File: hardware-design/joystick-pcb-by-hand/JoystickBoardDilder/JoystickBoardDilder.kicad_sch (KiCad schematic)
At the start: 2 parts, among them SW1 K1-1506SN-01, SW1Header1 Conn_01x06_Pin

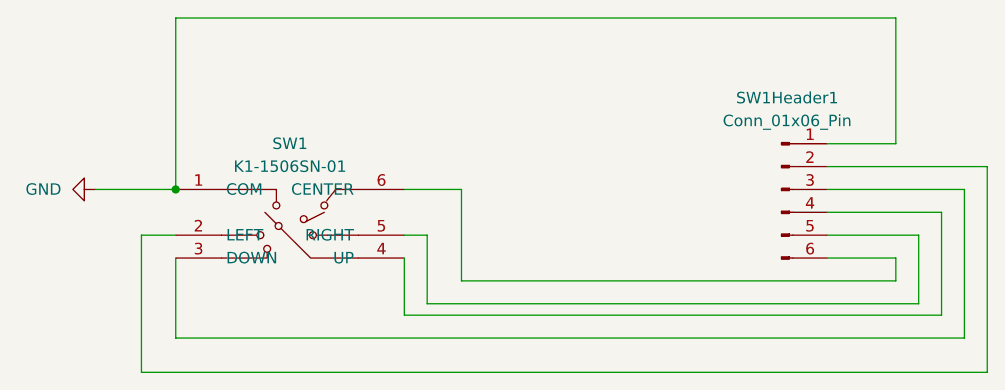
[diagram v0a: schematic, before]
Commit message: Joystick anchor pad, piezo speaker ring, MPU-6500 IMU pocket, alignment fix
- Replace JoyWell/Cut_JoyBody with 14x14mm anchor pad (12mm inner hole),
  extends from face_bot to PCB top (6.85mm depth)
- Fix joystick PCB Y placement: remove double-applied SW1 offset
  (stick now 0.01mm from hole center instead of 0.68mm off)
- Tighten cradle pit from 23mm to 20mm (0.2mm/side clearance for 19.6mm board)
- Add 20mm piezo speaker retaining ring on base plate (22.2mm OD, 1mm wall)
- Add MPU-6500 GY-6500 IMU rectangular pocket on base plate (25.4x15.4mm)
- Add procedural piezo disc and IMU module Part::Feature models
- Remove Cut_JoyBody, JoyWell, Cut_JoyPCBPocket, PicoRetentionBlock, TP4056_USBC
- Update render_views.FCMacro with sensor detail views
- New blog post: joystick-anchor-piezo-imu-sensors.md
- Update website home page with sensor build progress

Co-Authored-By: Claude Opus 4.6 (1M context) <noreply@anthropic.com>
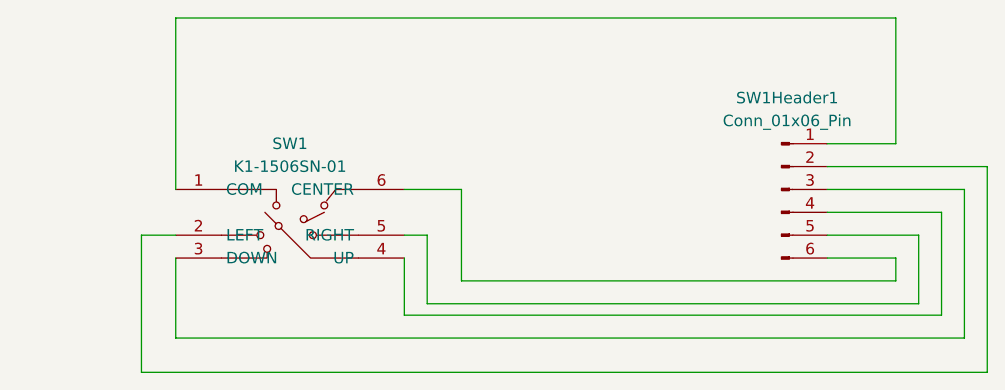
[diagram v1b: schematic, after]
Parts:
- SW1Header1: footprint (none) -> Connector_PinHeader_2.54mm:PinHeader_1x06_P2.54mm_Vertical
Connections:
- net GND: no longer names the net of SW1.1 (COM), SW1Header1.1 (COM)
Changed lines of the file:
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@@
 		(comment 1 "THis is my first board dont judge me")
 	)
-	(junction
-		(at 86.36 82.55)
-		(diameter 0)
-		(color 0 0 0 0)
-	)
 	(wire
 		(pts
@@
 		(pts
 			(xy 118.11 92.71) (xy 166.37 92.71)
-		)
-		(stroke
-			(width 0)
-			(type default)
-		)
-	)
-	(wire
-		(pts
-			(xy 77.47 82.55) (xy 86.36 82.55)
 		)
 		(stroke
@@
 			)
 		)
-		(property "Footprint" ""
+		(property "Footprint" "Connector_PinHeader_2.54mm:PinHeader_1x06_P2.54mm_Vertical"
 			(at 153.67 82.55 0)
 			(hide yes)
@@
 					(unit 1)
 				)
-			)
-		)
-	)
-	(symbol
-		(lib_id "power:GND")
-		(at 77.47 82.55 270)
-		(unit 1)
-		(body_style 1)
-		(exclude_from_sim no)
-		(in_bom yes)
-		(on_board yes)
-		(in_pos_files yes)
-		(dnp no)
-		(fields_autoplaced yes)
-		(property "Reference" "#PWR03"
-			(at 71.12 82.55 0)
-			(hide yes)
-			(show_name no)
-			(do_not_autoplace no)
-			(effects
-				(font
-					(size 1.27 1.27)
-				)
-			)
-		)
-		(property "Value" "GND"
-			(at 73.66 82.5499 90)
-			(show_name no)
-			(do_not_autoplace no)
-			(effects
-				(font
-					(size 1.27 1.27)
-				)
-				(justify right)
-			)
-		)
-		(property "Footprint" ""
-			(at 77.47 82.55 0)
-			(hide yes)
-			(show_name no)
-			(do_not_autoplace no)
-			(effects
-				(font
-					(size 1.27 1.27)
-				)
-			)
-		)
-		(property "Datasheet" ""
-			(at 77.47 82.55 0)
-			(hide yes)
-			(show_name no)
-			(do_not_autoplace no)
-			(effects
-				(font
-					(size 1.27 1.27)
-				)
-			)
-		)
-		(property "Description" "Power symbol creates a global label with name \"GND\" , ground"
-			(at 77.47 82.55 0)
-			(hide yes)
-			(show_name no)
-			(do_not_autoplace no)
-			(effects
-				(font
-					(size 1.27 1.27)
-				)
-			)
-		)
-		(pin "1"
-		)
-		(instances
-			(project "JoystickBoardDilder"
-				(path "/b688b85e-9c1d-49d3-8ae8-b37035f26fb0"
-					(reference "#PWR03")
-					(unit 1)
-				)
